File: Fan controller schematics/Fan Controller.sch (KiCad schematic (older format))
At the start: 11 parts, among them IC1 ATMEGA328-P, SW1 ROTARY_ENCODER, U1 LM385-1.25, Y1 16MHz

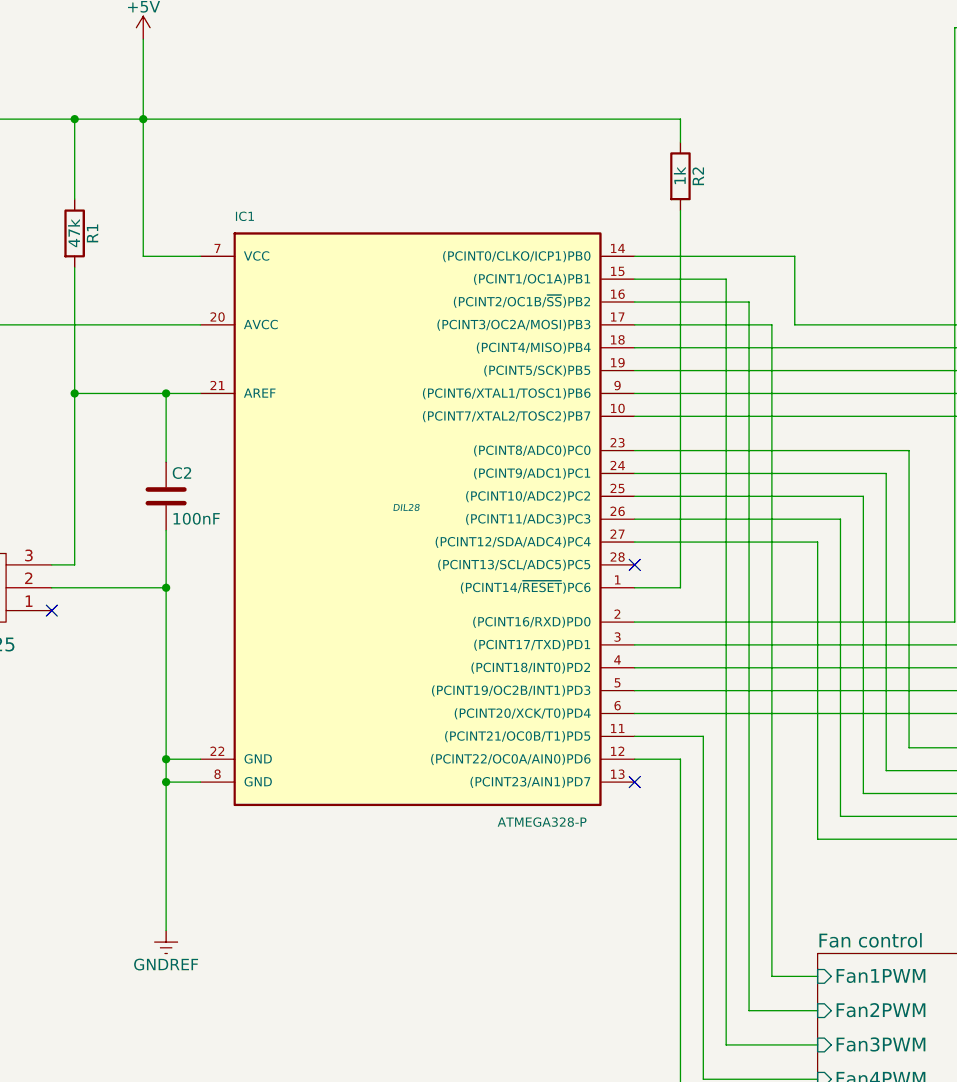
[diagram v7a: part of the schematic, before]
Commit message: Update schematic to v1.3
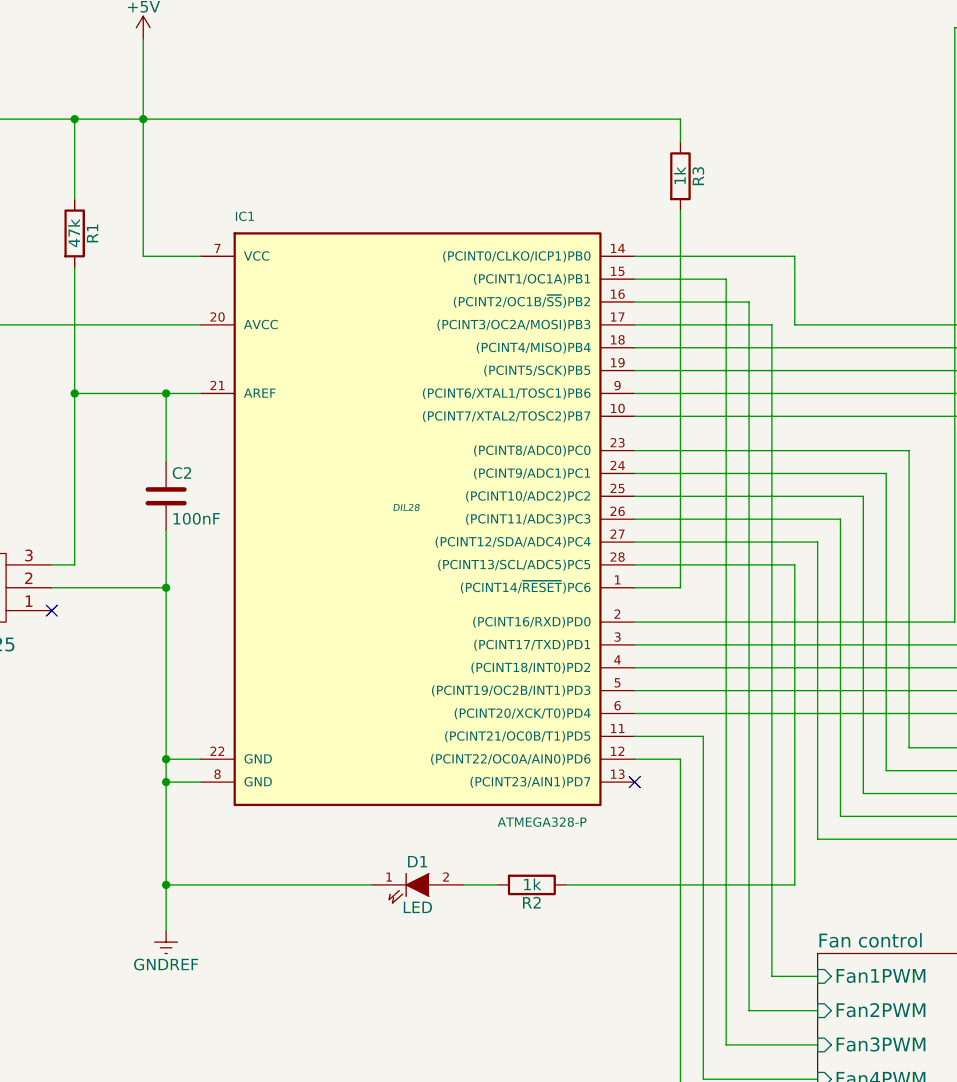
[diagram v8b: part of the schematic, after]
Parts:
- added D1: LED, symbol LED
- added R2: 1k, symbol R
- renumbered R2 to R3
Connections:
- net GNDREF: now also D1.1 (K)
- net at IC1.28 ((PCINT13/SCL/ADC5)PC5): now also R2.1
- new net: D1.2 (A), R2.2
- no-connect marks 3 -> 2
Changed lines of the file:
@@
 Sheet 1 3
 Title "Fan Controller for PC"
-Date "2016-09-14"
+Date "2016-12-10"
 Rev "1.3"
 Comp "Dahlström Electronics"
@@
 $EndComp
 $Comp
-L +5V #PWR2
+L +5V #PWR01
 U 1 1 57C31247
 P 1750 1850
-F 0 "#PWR2" H 1750 1700 50  0001 C CNN
+F 0 "#PWR01" H 1750 1700 50  0001 C CNN
 F 1 "+5V" H 1750 1990 50  0000 C CNN
 F 2 "" H 1750 1850 60  0000 C CNN
@@
 $EndComp
 $Comp
-L GNDREF #PWR3
+L GNDREF #PWR02
 U 1 1 57C31302
 P 1850 5750
-F 0 "#PWR3" H 1850 5500 50  0001 C CNN
+F 0 "#PWR02" H 1850 5500 50  0001 C CNN
 F 1 "GNDREF" H 1850 5600 50  0000 C CNN
 F 2 "" H 1850 5750 60  0000 C CNN
@@
 $EndComp
 $Comp
-L GNDREF #PWR4
+L GNDREF #PWR03
 U 1 1 57DB07CE
 P 6000 4600
-F 0 "#PWR4" H 6000 4350 50  0001 C CNN
+F 0 "#PWR03" H 6000 4350 50  0001 C CNN
 F 1 "GNDREF" H 6000 4450 50  0000 C CNN
 F 2 "" H 6000 4600 60  0000 C CNN
@@
 $EndComp
 $Comp
-L GNDREF #PWR5
+L GNDREF #PWR04
 U 1 1 57DB0842
 P 6700 4600
-F 0 "#PWR5" H 6700 4350 50  0001 C CNN
+F 0 "#PWR04" H 6700 4350 50  0001 C CNN
 F 1 "GNDREF" H 6700 4450 50  0000 C CNN
 F 2 "" H 6700 4600 60  0000 C CNN
@@
 $EndComp
 $Comp
-L R R2
+L R R3
 U 1 1 57DBCB8F
 P 4100 2450
-F 0 "R2" V 4180 2450 50  0000 C CNN
+F 0 "R3" V 4180 2450 50  0000 C CNN
 F 1 "1k" V 4100 2450 50  0000 C CNN
 F 2 "" V 4030 2450 50  0000 C CNN
@@
 	1850 4000 1850 5750
 Wire Wire Line
-	2000 5100 1850 5100
-Connection ~ 1850 5100
-Wire Wire Line
 	850  3100 2000 3100
 Wire Wire Line
@@
 	3900 3200 7350 3200
 $Comp
-L GNDREF #PWR6
+L GNDREF #PWR05
 U 1 1 57D90A53
 P 7450 3400
-F 0 "#PWR6" H 7450 3150 50  0001 C CNN
+F 0 "#PWR05" H 7450 3150 50  0001 C CNN
 F 1 "GNDREF" H 7450 3250 50  0000 C CNN
 F 2 "" H 7450 3400 60  0000 C CNN
@@
 	7350 3100 7850 3100
 $Comp
-L GNDREF #PWR7
+L GNDREF #PWR06
 U 1 1 57D90E03
 P 8750 3400
-F 0 "#PWR7" H 8750 3150 50  0001 C CNN
+F 0 "#PWR06" H 8750 3150 50  0001 C CNN
 F 1 "GNDREF" H 8750 3250 50  0000 C CNN
 F 2 "" H 8750 3400 60  0000 C CNN
@@
 	1750 1850 1750 2800
 $Comp
-L GNDREF #PWR1
+L GNDREF #PWR07
 U 1 1 57D95279
 P 850 3700
-F 0 "#PWR1" H 850 3450 50  0001 C CNN
+F 0 "#PWR07" H 850 3450 50  0001 C CNN
 F 1 "GNDREF" H 850 3550 50  0000 C CNN
 F 2 "" H 850 3700 60  0000 C CNN
@@
 Connection ~ 1850 4250
 NoConn ~ 3900 5100
-NoConn ~ 3900 4150
 NoConn ~ 1350 4350
+$Comp
+L LED D1
+U 1 1 584C2FAE
+P 2950 5550
+F 0 "D1" H 2950 5650 50  0000 C CNN
+F 1 "LED" H 2950 5450 50  0000 C CNN
+F 2 "" H 2950 5550 50  0000 C CNN
+F 3 "" H 2950 5550 50  0000 C CNN
+	1    2950 5550
+	1    0    0    -1
+$EndComp
+$Comp
+L R R2
+U 1 1 584C3061
+P 3450 5550
+F 0 "R2" V 3530 5550 50  0000 C CNN
+F 1 "1k" V 3450 5550 50  0000 C CNN
+F 2 "" V 3380 5550 50  0000 C CNN
+F 3 "" H 3450 5550 50  0000 C CNN
+	1    3450 5550
+	0    1    1    0
+$EndComp
+Wire Wire Line
+	3300 5550 3150 5550
+Wire Wire Line
+	2750 5550 1850 5550
+Connection ~ 1850 5550
+Wire Wire Line
+	3600 5550 4600 5550
+Wire Wire Line
+	4600 5550 4600 4150
+Wire Wire Line
+	4600 4150 3900 4150
+Wire Wire Line
+	2000 5100 1850 5100
+Connection ~ 1850 5100
 $EndSCHEMATC
